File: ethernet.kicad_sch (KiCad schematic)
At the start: 40 parts, among them U7 LAN8720A, U8 ARJM11C7-114-BA-EW2, Y2 Crystal_GND24

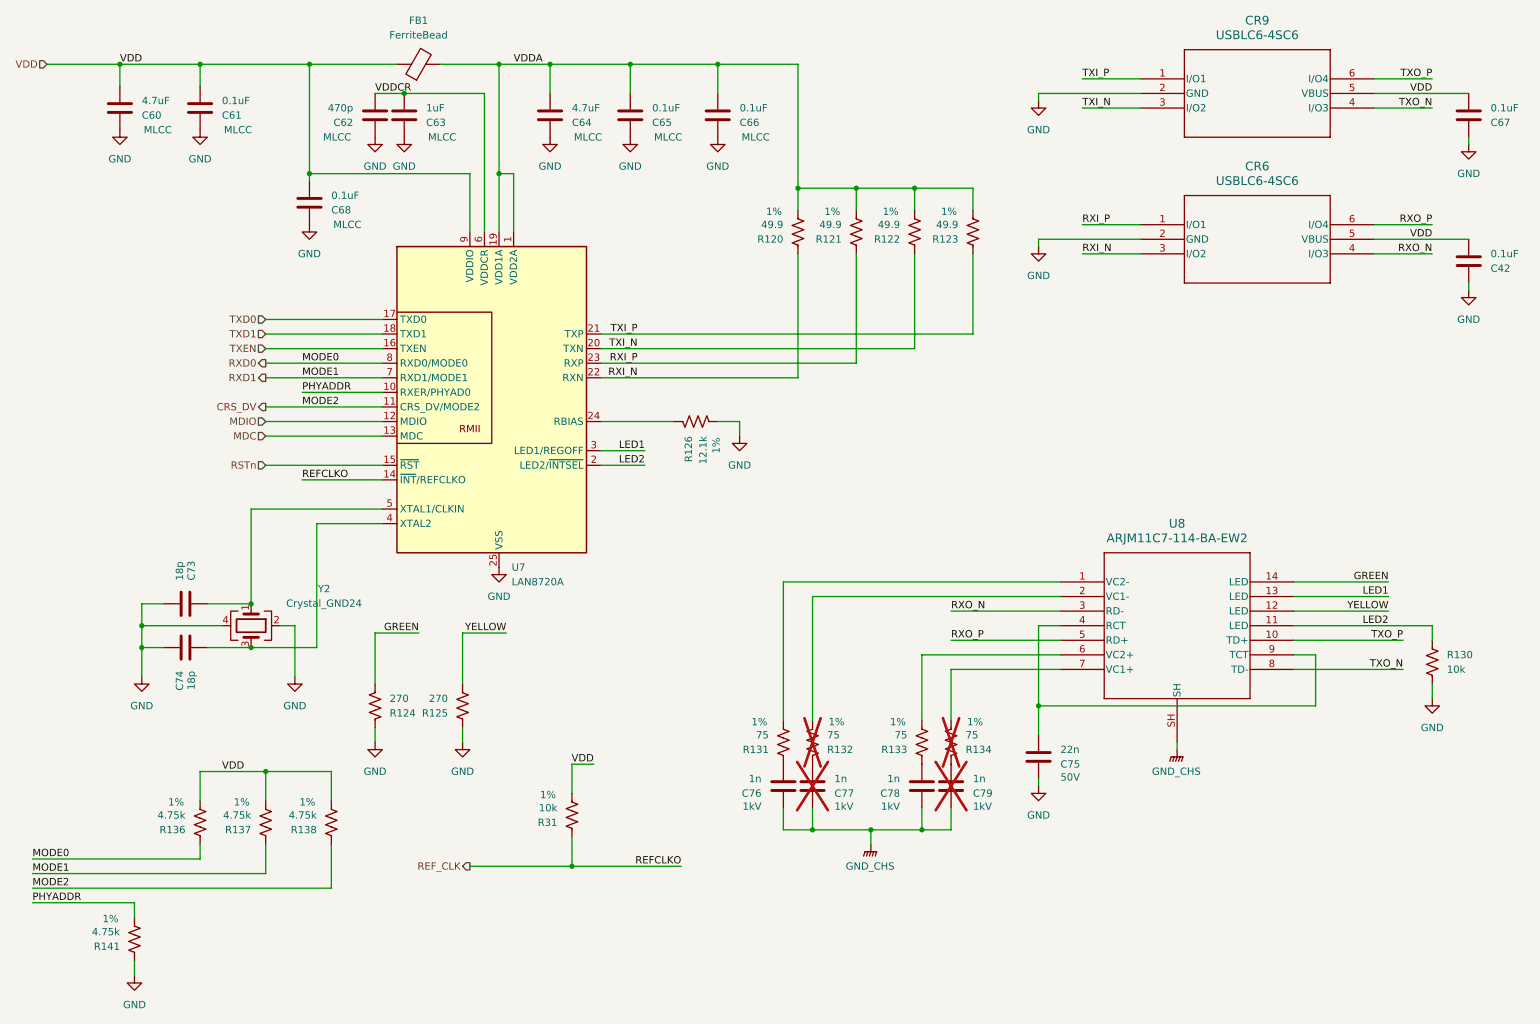
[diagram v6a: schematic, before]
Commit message: Organizing REFDES
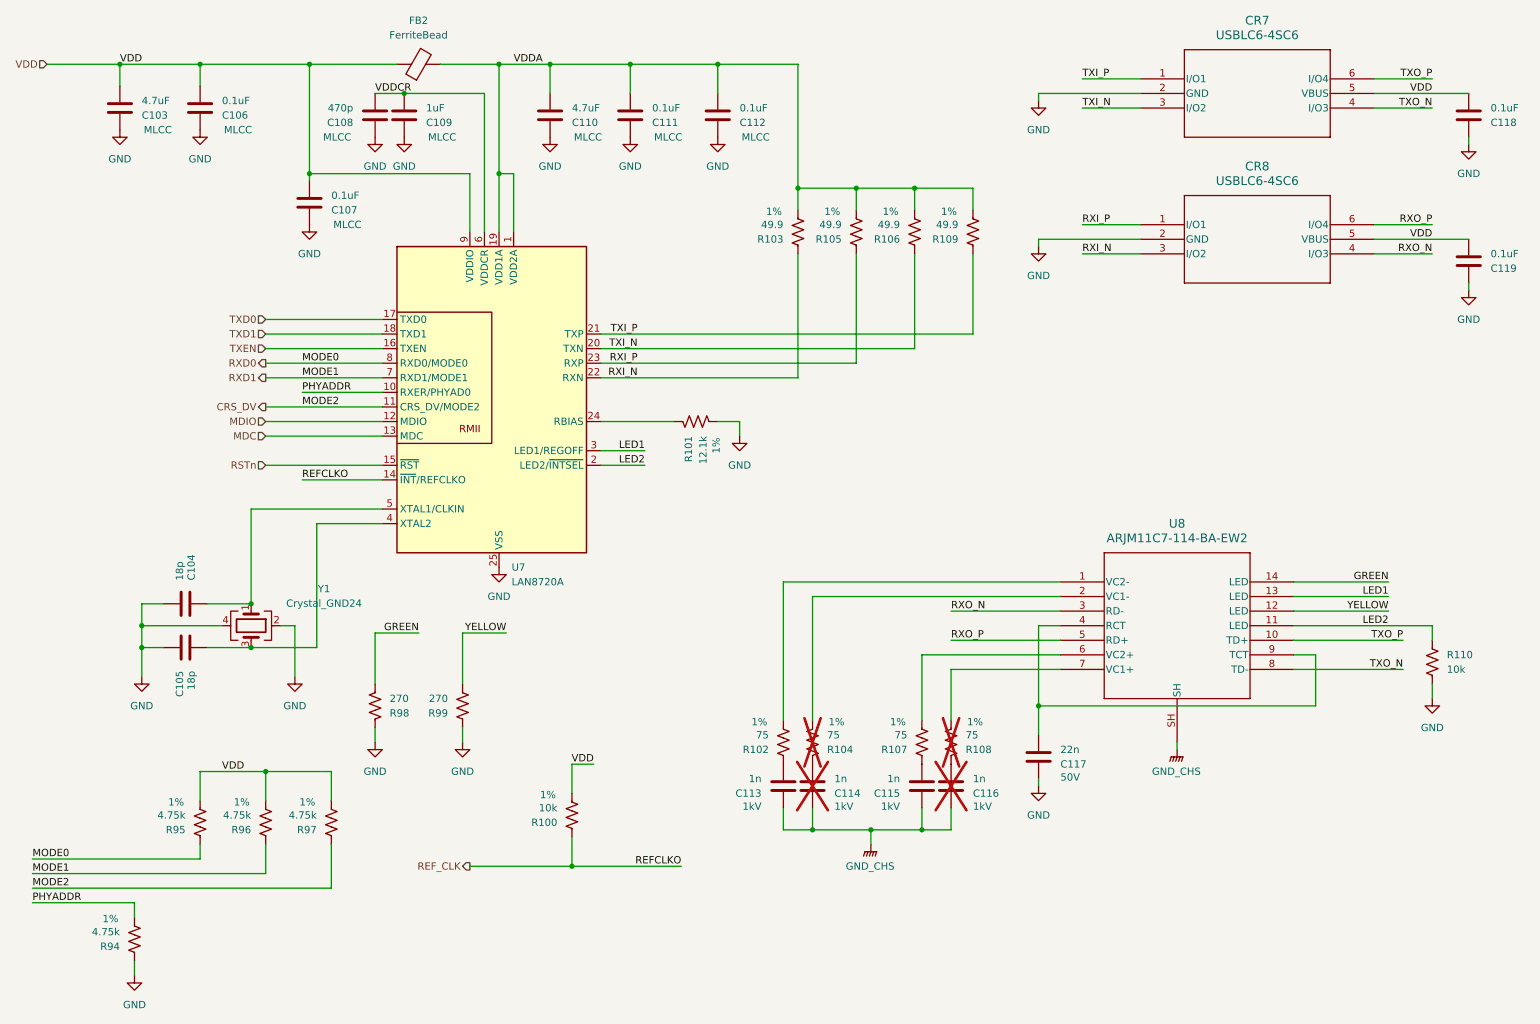
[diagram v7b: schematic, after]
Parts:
- renumbered C60 to C103, C73 to C104, C74 to C105, C61 to C106, C68 to C107, C62 to C108, C63 to C109, C64 to C110, C65 to C111, C66 to C112, C76 to C113, C77 to C114, C78 to C115, C79 to C116, C75 to C117, C67 to C118, C42 to C119, CR9 to CR7, CR6 to CR8, FB1 to FB2, R31 to R100, R126 to R101, R131 to R102, R120 to R103, R132 to R104, R121 to R105, R122 to R106, R133 to R107, R134 to R108, R123 to R109, R130 to R110, R141 to R94, R136 to R95, R137 to R96, R138 to R97, R124 to R98, R125 to R99, Y2 to Y1
